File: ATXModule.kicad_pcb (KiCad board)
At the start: 2 copper layers, 88 x 56 mm, 18 parts, among them J1 Screw_Terminal_01x02, J2 Screw_Terminal_01x02, J3 Screw_Terminal_01x02, J4 Conn_01x02_Pin, Q1 2N2222A, Q2 2N2222A

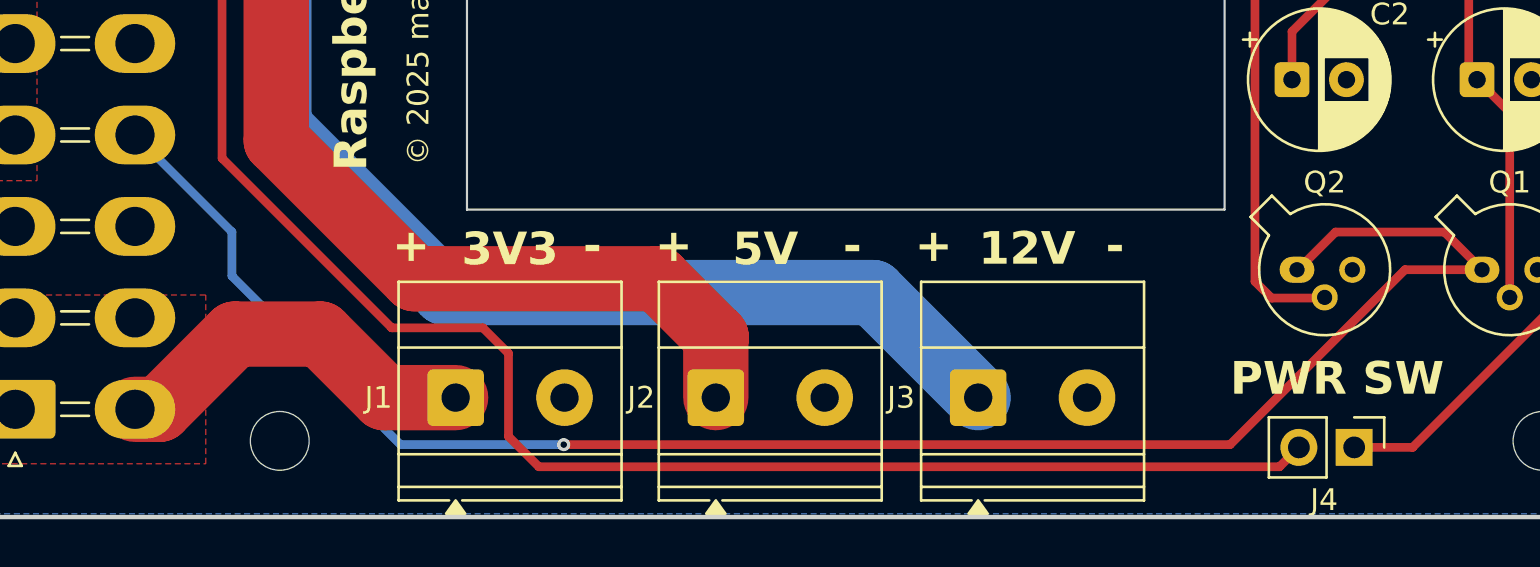
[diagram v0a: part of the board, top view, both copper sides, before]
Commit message: PCB: improved some tracks placement
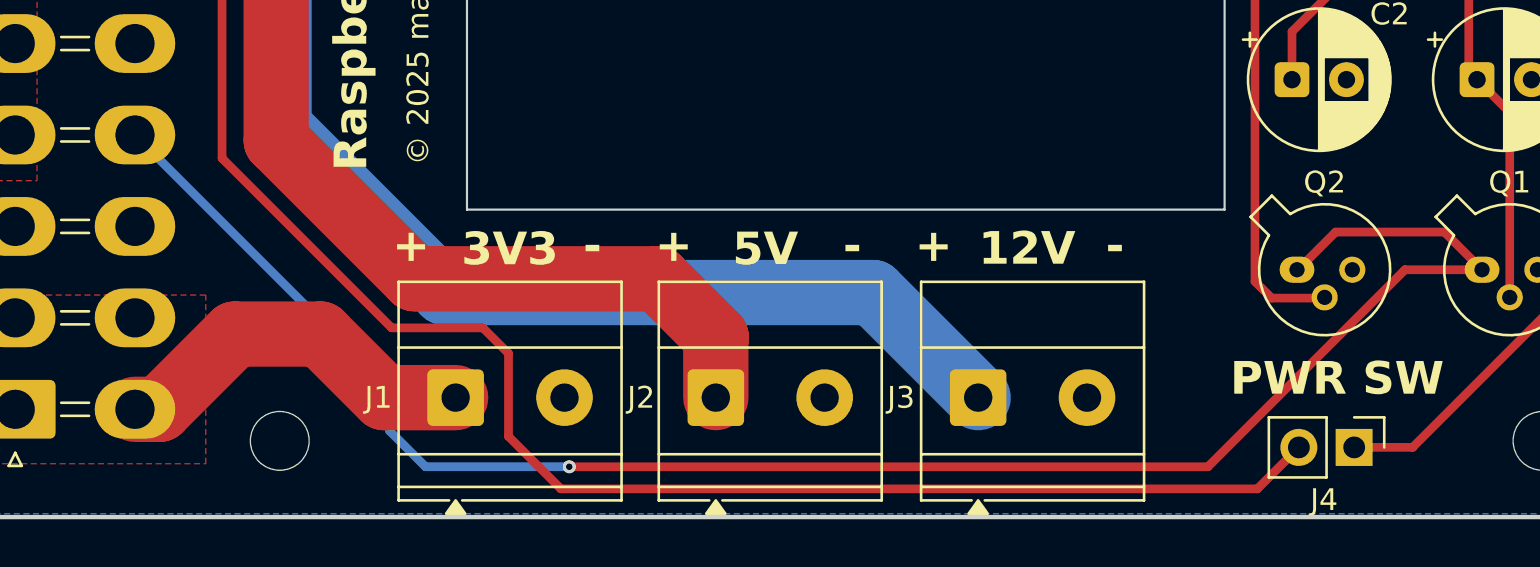
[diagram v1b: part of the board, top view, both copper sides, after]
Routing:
- net ATX_5VSB: track 86.0 -> 86.8 mm
- net ATX_PS-ON: track 82.2 -> 83.0 mm
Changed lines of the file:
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@@
+	)
+	(segment
+		(start 115.539236 121.508236)
+		(end 119.730236 121.508236)
+		(width 0.4)
+		(layer "F.Cu")
+		(net 6)
+	)
+	(segment
+		(start 101 97)
+		(end 102 98)
+		(width 0.4)
+		(layer "F.Cu")
+		(net 6)
+	)
+	(segment
+		(start 101 94.4)
+		(end 101 97)
+		(width 0.4)
+		(layer "F.Cu")
+		(net 6)
+	)
+	(segment
+		(start 120.904 126.492)
+		(end 123.317 128.905)
+		(width 0.4)
+		(layer "F.Cu")
+		(net 6)
+	)
+	(segment
+		(start 102 98)
+		(end 105.5 98)
+		(width 0.4)
+		(layer "F.Cu")
+		(net 6)
+	)
+	(segment
+		(start 155.305 128.905)
+		(end 157.21 127)
+		(width 0.4)
+		(layer "F.Cu")
+		(net 6)
+	)
+	(segment
+		(start 107.75 100.25)
+		(end 107.75 113.719)
+		(width 0.4)
+		(layer "F.Cu")
+		(net 6)
 	)
 	(segment
@@
 	)
 	(segment
-		(start 156.321 127.889)
-		(end 157.21 127)
+		(start 107.75 113.719)
+		(end 115.539236 121.508236)
 		(width 0.4)
 		(layer "F.Cu")
@@
 	)
 	(segment
-		(start 122.301 127.889)
-		(end 156.321 127.889)
-		(width 0.4)
-		(layer "F.Cu")
-		(net 6)
-	)
-	(segment
-		(start 107.75 113.719)
-		(end 115.539236 121.508236)
+		(start 123.317 128.905)
+		(end 155.305 128.905)
 		(width 0.4)
 		(layer "F.Cu")
@@
 	)
 	(segment
-		(start 115.539236 121.508236)
-		(end 119.730236 121.508236)
-		(width 0.4)
-		(layer "F.Cu")
-		(net 6)
-	)
-	(segment
-		(start 107.75 100.25)
-		(end 107.75 113.719)
-		(width 0.4)
-		(layer "F.Cu")
-		(net 6)
-	)
-	(segment
-		(start 102 98)
-		(end 105.5 98)
-		(width 0.4)
-		(layer "F.Cu")
-		(net 6)
-	)
-	(segment
-		(start 120.904 126.492)
-		(end 122.301 127.889)
-		(width 0.4)
-		(layer "F.Cu")
-		(net 6)
-	)
-	(segment
-		(start 101 94.4)
-		(end 101 97)
-		(width 0.4)
-		(layer "F.Cu")
-		(net 6)
-	)
-	(segment
-		(start 101 97)
-		(end 102 98)
-		(width 0.4)
-		(layer "F.Cu")
-		(net 6)
-	)
-	(segment
-		(start 123.444 126.873)
-		(end 154.051 126.873)
+		(start 123.698 127.889)
+		(end 153.035 127.889)
 		(width 0.4)
 		(layer "F.Cu")
@@
 	)
 	(segment
+		(start 153.035 127.889)
+		(end 162.085 118.839)
+		(width 0.4)
+		(layer "F.Cu")
+		(net 8)
+	)
+	(segment
 		(start 157.164 118.839)
 		(end 158.894 117.109)
@@
 		(net 8)
 	)
-	(segment
-		(start 154.051 126.873)
-		(end 162.085 118.839)
-		(width 0.4)
-		(layer "F.Cu")
-		(net 8)
-	)
 	(via
-		(at 123.444 126.873)
+		(at 123.698 127.889)
 		(size 0.6)
 		(drill 0.3)
@@
 	)
 	(segment
-		(start 108.204 119.126)
-		(end 108.204 117.104)
+		(start 115.443 126.238)
+		(end 115.443 124.343)
 		(width 0.4)
 		(layer "B.Cu")
@@
 	)
 	(segment
-		(start 108.204 117.104)
+		(start 115.443 124.343)
 		(end 103.75 112.65)
 		(width 0.4)
@@
 	)
 	(segment
-		(start 115.951 126.873)
-		(end 108.204 119.126)
+		(start 117.094 127.889)
+		(end 115.443 126.238)
 		(width 0.4)
 		(layer "B.Cu")
@@
 	)
 	(segment
-		(start 123.444 126.873)
-		(end 115.951 126.873)
+		(start 123.698 127.889)
+		(end 117.094 127.889)
 		(width 0.4)
 		(layer "B.Cu")

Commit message: Add project page QR code silkscreen
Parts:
- added G1: LOGO, qr:qr, B.Cu at (90.6, 102.1)

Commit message: Update PCB
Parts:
- C2: value 47u -> 33u
- R1: value 10k -> 300k
- R2: value 18k -> 470k
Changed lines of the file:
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@@
 			)
 		)
-		(property "Value" "18k"
+		(property "Value" "470k"
 			(at 5.08 2.37 0)
 			(layer "F.Fab")
@@
 			)
 		)
-		(property "Value" "47u"
+		(property "Value" "33u"
 			(at 1.25 4.4 0)
 			(layer "F.Fab")
@@
 			)
 		)
-		(property "Value" "10k"
+		(property "Value" "300k"
 			(at 5.08 2.37 0)
 			(layer "F.Fab")

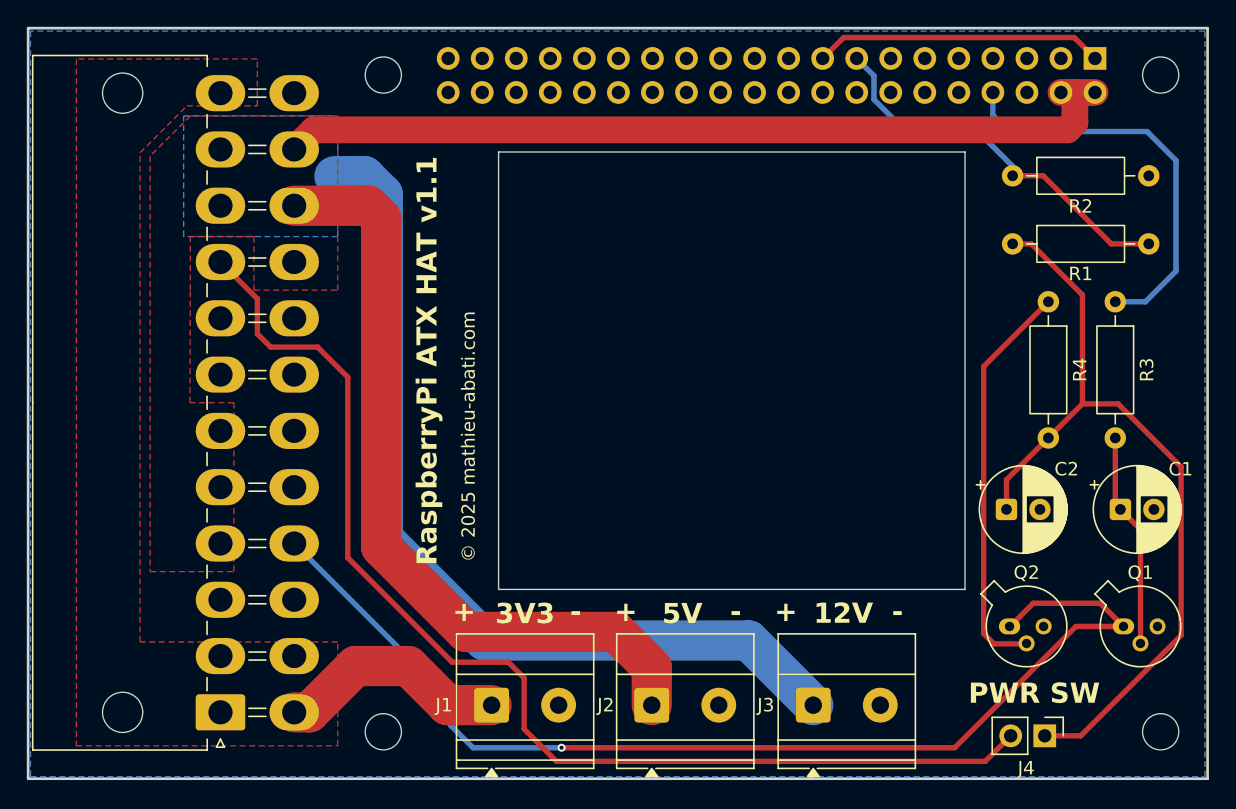
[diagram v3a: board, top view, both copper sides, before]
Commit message: Add fan footprint, screw holes and connectors
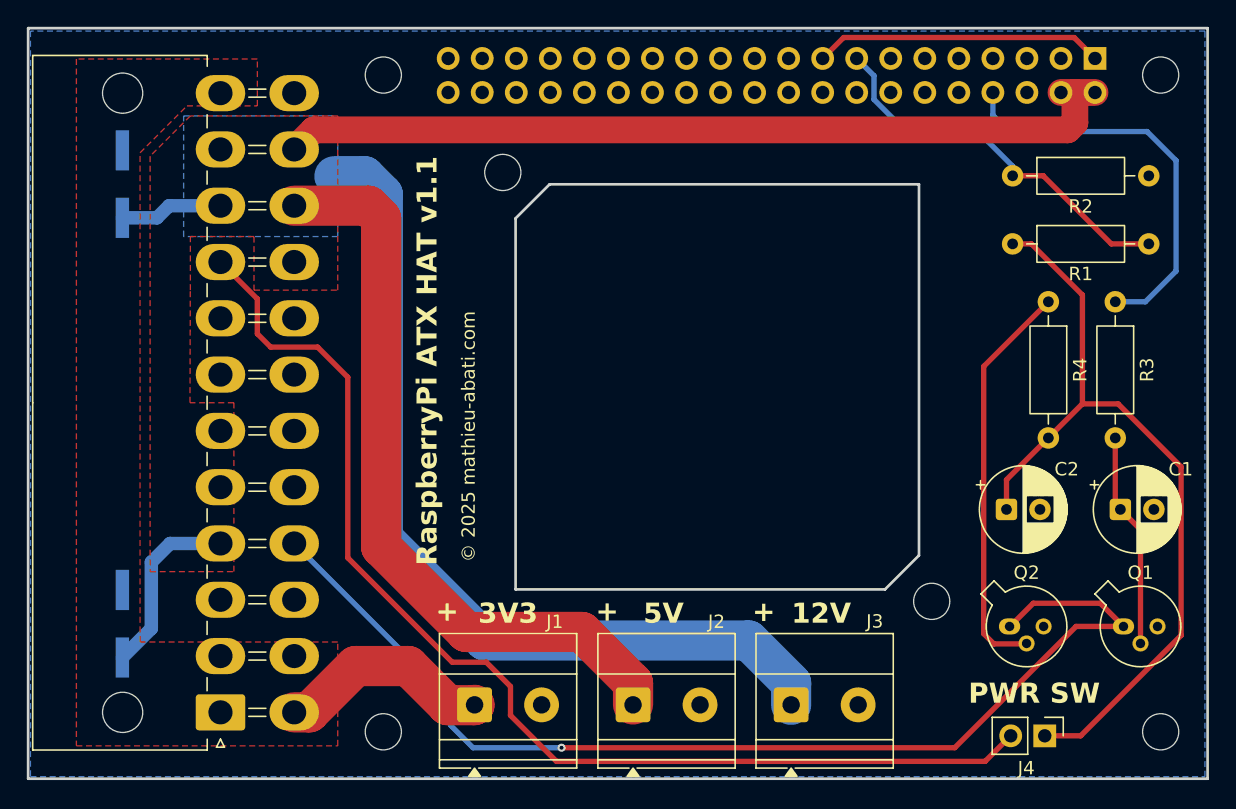
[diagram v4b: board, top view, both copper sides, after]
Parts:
- added ?: , , F.Cu at (122.3, 85.6)
- added ?: , , F.Cu at (150.1, 117.0)
- added J5: Conn_01x02_Pin, Connector_PinSocket_2.54mm:PinSocket_2x01_P2.54mm_Vertical_SMD, B.Cu at (90.9, 85.8)
- added J6: Conn_01x02_Pin, Connector_PinSocket_2.54mm:PinSocket_2x01_P2.54mm_Vertical_SMD, B.Cu at (90.9, 118.6)
- moved J3 1.65 mm to (140.8, 124.7)
- moved J2 1.40 mm to (129.0, 124.7)
- moved J1 1.27 mm to (117.2, 124.7)
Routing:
- net +5V: track 122.0 -> 133.6 mm
- net ATX_12V: track 67.1 -> 74.1 mm
- net ATX_3V3: track 17.4 -> 16.1 mm
- net ATX_5VSB: track 86.8 -> 85.9 mm
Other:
- outline, holes or cut-outs redrawn
- board text added: "Fan"
- board text added: "Fan 12V"
- board text added: "Fan 5V"
- board text removed: "-"
